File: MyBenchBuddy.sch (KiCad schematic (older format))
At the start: 0 parts

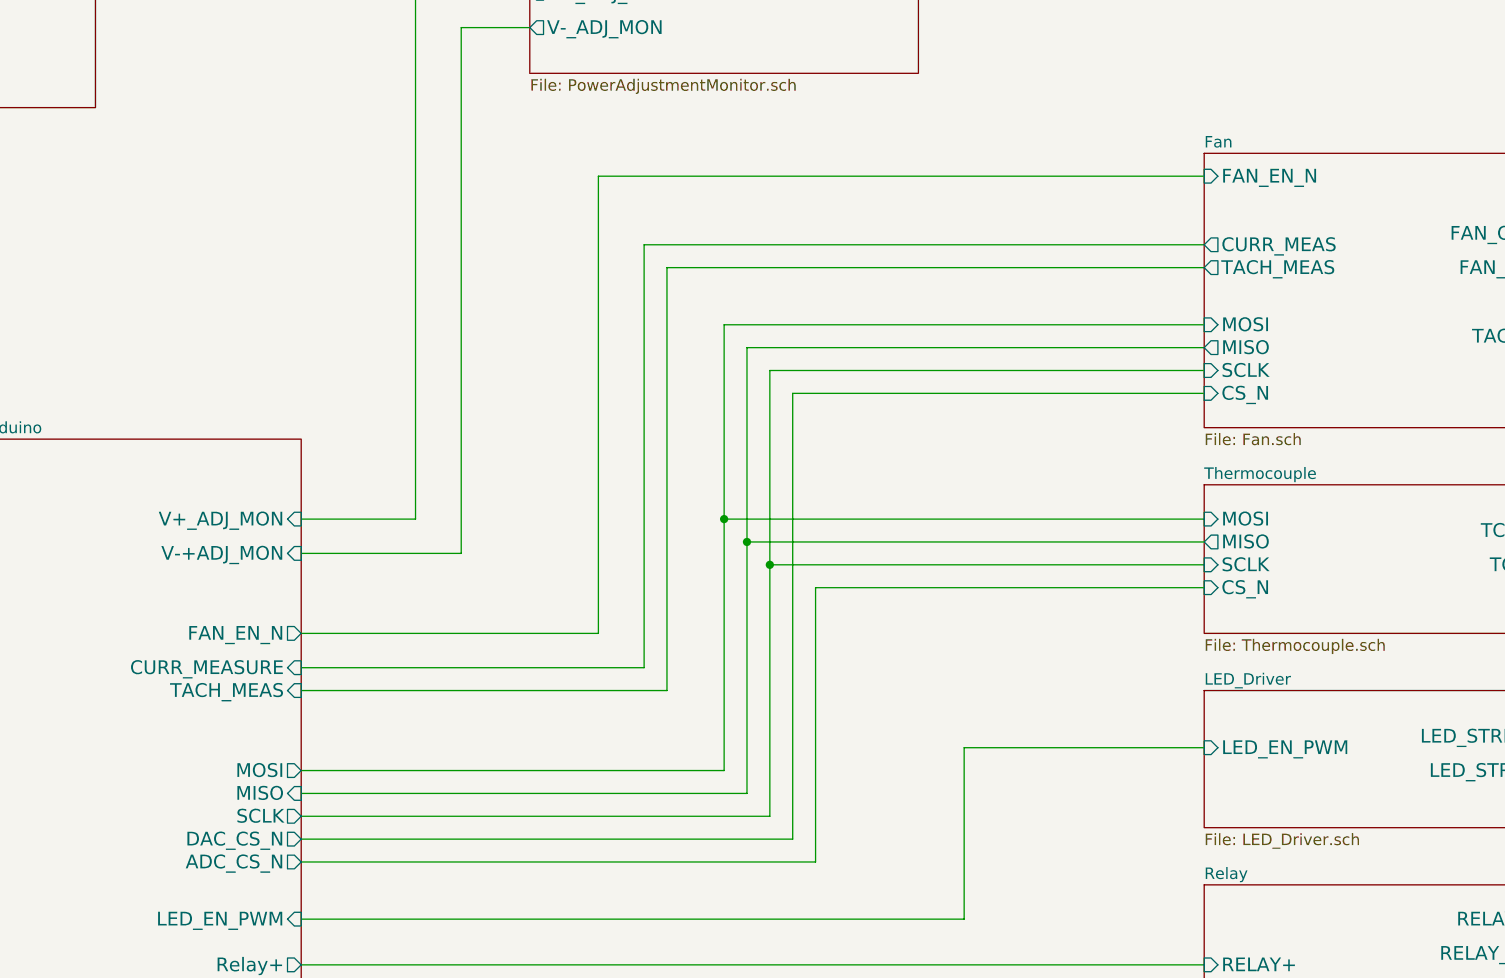
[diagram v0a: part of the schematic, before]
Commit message: Fan/Current Module Rework
Rework of the Fan/Current module
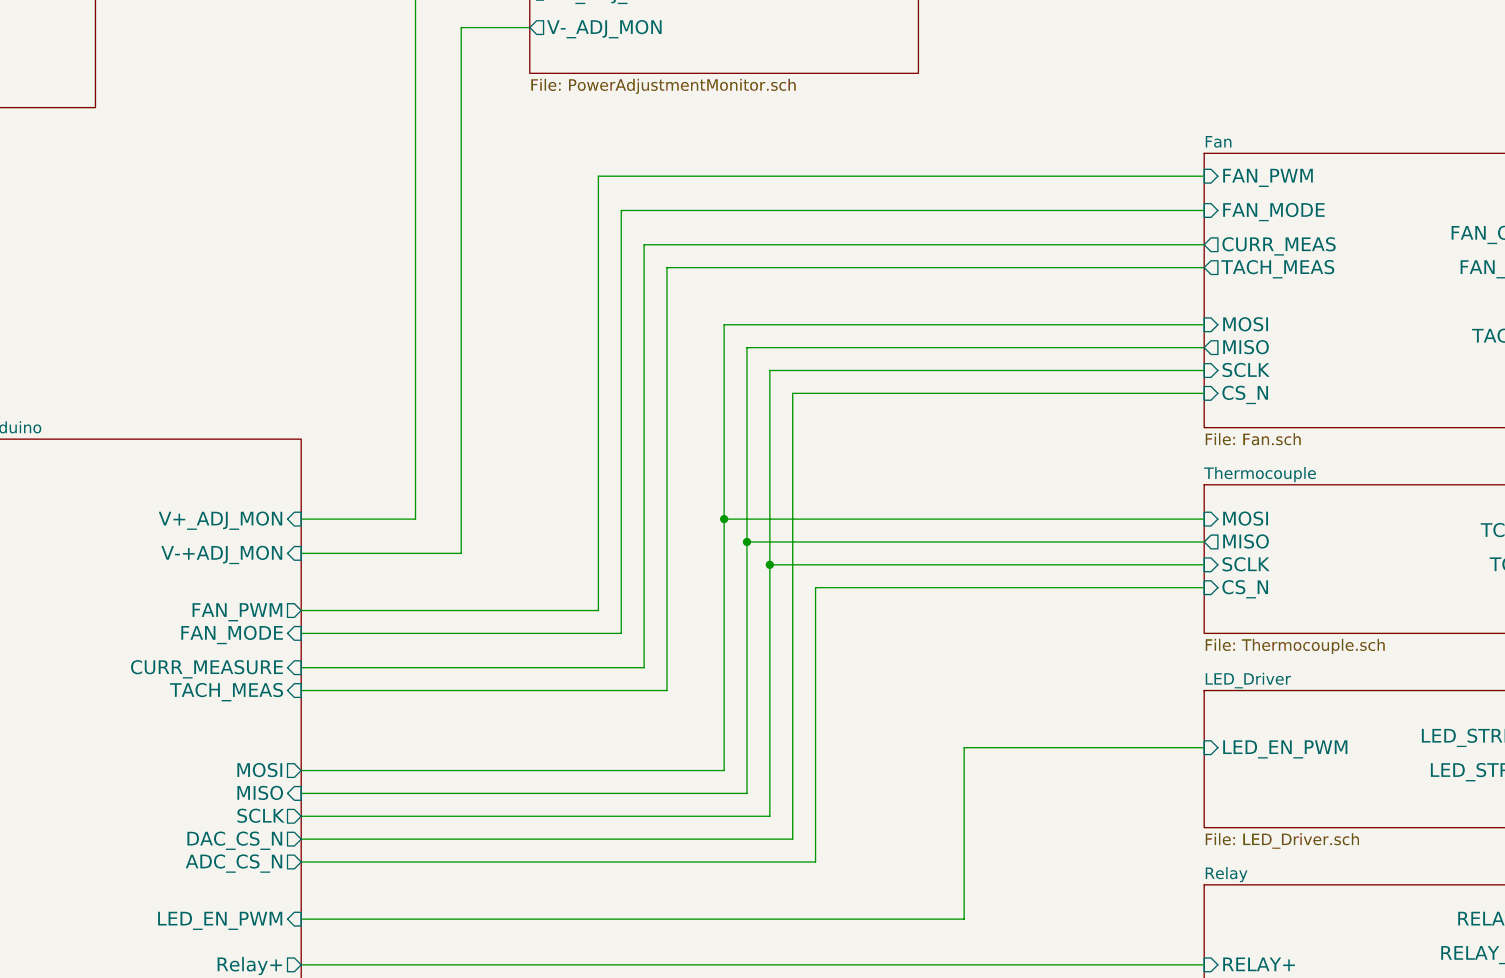
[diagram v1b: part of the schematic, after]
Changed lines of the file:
@@
 F7 "TACH_IN" I R 9500 3450 60
 F8 "TACH_MEAS" O L 7900 3150 60
-F9 "FAN_EN_N" I L 7900 2750 60
-F10 "CURR_MEAS" O L 7900 3050 60
-F11 "FAN_OUT-" O R 9500 3150 60
+F9 "CURR_MEAS" O L 7900 3050 60
+F10 "FAN_OUT-" O R 9500 3150 60
+F11 "FAN_MODE" I L 7900 2900 60
+F12 "FAN_PWM" I L 7900 2750 60
 $EndSheet
 $Sheet
@@
 	4650 2100 4950 2100
 Wire Wire Line
-	3950 4750 5250 4750
+	3950 4650 5250 4650
 Wire Wire Line
-	5250 4750 5250 2750
+	5250 4650 5250 2750
 Wire Wire Line
 	5250 2750 7900 2750
@@
 F6 "SCLK" O R 3950 5550 60
 F7 "TACH_MEAS" I R 3950 5000 60
-F8 "FAN_EN_N" O R 3950 4750 60
-F9 "CURR_MEASURE" I R 3950 4900 60
-F10 "V+_ADJ_MON" I R 3950 4250 60
-F11 "V-+ADJ_MON" I R 3950 4400 60
-F12 "LED_EN_PWM" I R 3950 6000 60
-F13 "DAC_CS_N" O R 3950 5650 60
-F14 "ADC_CS_N" O R 3950 5750 60
+F8 "CURR_MEASURE" I R 3950 4900 60
+F9 "V+_ADJ_MON" I R 3950 4250 60
+F10 "V-+ADJ_MON" I R 3950 4400 60
+F11 "LED_EN_PWM" I R 3950 6000 60
+F12 "DAC_CS_N" O R 3950 5650 60
+F13 "ADC_CS_N" O R 3950 5750 60
+F14 "FAN_PWM" O R 3950 4650 60
+F15 "FAN_MODE" I R 3950 4750 60
 $EndSheet
 Wire Wire Line
-	3950 5350 5800 5350
+	5800 5350 3950 5350
 Wire Wire Line
-	5800 5350 5800 3400
+	5800 3400 5800 5350
 Wire Wire Line
 	5800 3400 7900 3400
 Wire Wire Line
-	3950 5450 5900 5450
+	5900 5450 3950 5450
 Wire Wire Line
-	5900 5450 5900 3500
+	5900 3500 5900 5450
 Wire Wire Line
 	5900 3500 7900 3500
 Wire Wire Line
-	3950 5550 6000 5550
+	6000 5550 3950 5550
 Wire Wire Line
-	6000 5550 6000 3600
+	6000 3600 6000 5550
 Wire Wire Line
 	6100 5650 3950 5650
@@
 Wire Wire Line
 	6200 4550 7900 4550
+Wire Wire Line
+	7900 2900 5350 2900
+Wire Wire Line
+	5350 2900 5350 4750
+Wire Wire Line
+	5350 4750 3950 4750
 $EndSCHEMATC

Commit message: Modified the Power Control module
Modified the Power Control module
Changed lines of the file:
@@
 Sheet 1 9
 Title ""
-Date "28 sep 2013"
+Date "27 nov 2013"
 Rev ""
 Comp ""
@@
 F12 "RELAY_NO" I L 10200 6300 60
 F13 "RELAY_NC" I L 10200 6000 60
-$EndSheet
-$Sheet
-S 4950 800  1700 1500
-U 523F9073
-F0 "PowerAdjustmentMonitor" 50
-F1 "PowerAdjustmentMonitor.sch" 50
-F2 "V+_ADJ" O R 6650 1100 60
-F3 "V-_ADJ" O R 6650 1300 60
-F4 "3V3_MON" O L 4950 1250 60
-F5 "5V_MON" O L 4950 1100 60
-F6 "V+_ADJ_MON" O L 4950 1950 60
-F7 "V-_ADJ_MON" O L 4950 2100 60
-F8 "V-_CURR_MON" O L 4950 1700 60
-F9 "V+_CURR_MON" O L 4950 1550 60
 $EndSheet
 $Sheet
@@
 Wire Wire Line
 	5350 4750 3950 4750
+$Sheet
+S 4950 800  1700 1500
+U 523F9073
+F0 "PowerAdjustmentMonitor" 50
+F1 "PowerAdjustmentMonitor.sch" 50
+F2 "V+_ADJ" O R 6650 1100 60
+F3 "V-_ADJ" O R 6650 1300 60
+F4 "3V3_MON" O L 4950 1250 60
+F5 "5V_MON" O L 4950 1100 60
+F6 "V+_ADJ_MON" O L 4950 1950 60
+F7 "V-_ADJ_MON" O L 4950 2100 60
+$EndSheet
 $EndSCHEMATC
